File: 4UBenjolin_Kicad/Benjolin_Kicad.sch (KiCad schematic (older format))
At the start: 127 parts, among them J1 Conn_01x04_Male, J10 MAINOUT, J11 PWM, J12 RUN, J13 XOR, J14 CV_1, J15 CV_2, J16 Mix_In_3, J17 Mix_In_4, J18 Mixer_Out, J2 Mix_In_1, J3 Mix_In_2, J4 EXT.INPUT, J5 CV_F, J6 PUL2, J7 TRI1, J8 TRI2, J9 PUL1, Q1 BC547, SW1 SW_SPDT, U1 TL074, U2 TL072, U3 TL074, U4 TL074, U5 SSI2164, U6 4021, U7 L78L09_SOT89, U8 79L09, U9 TL071

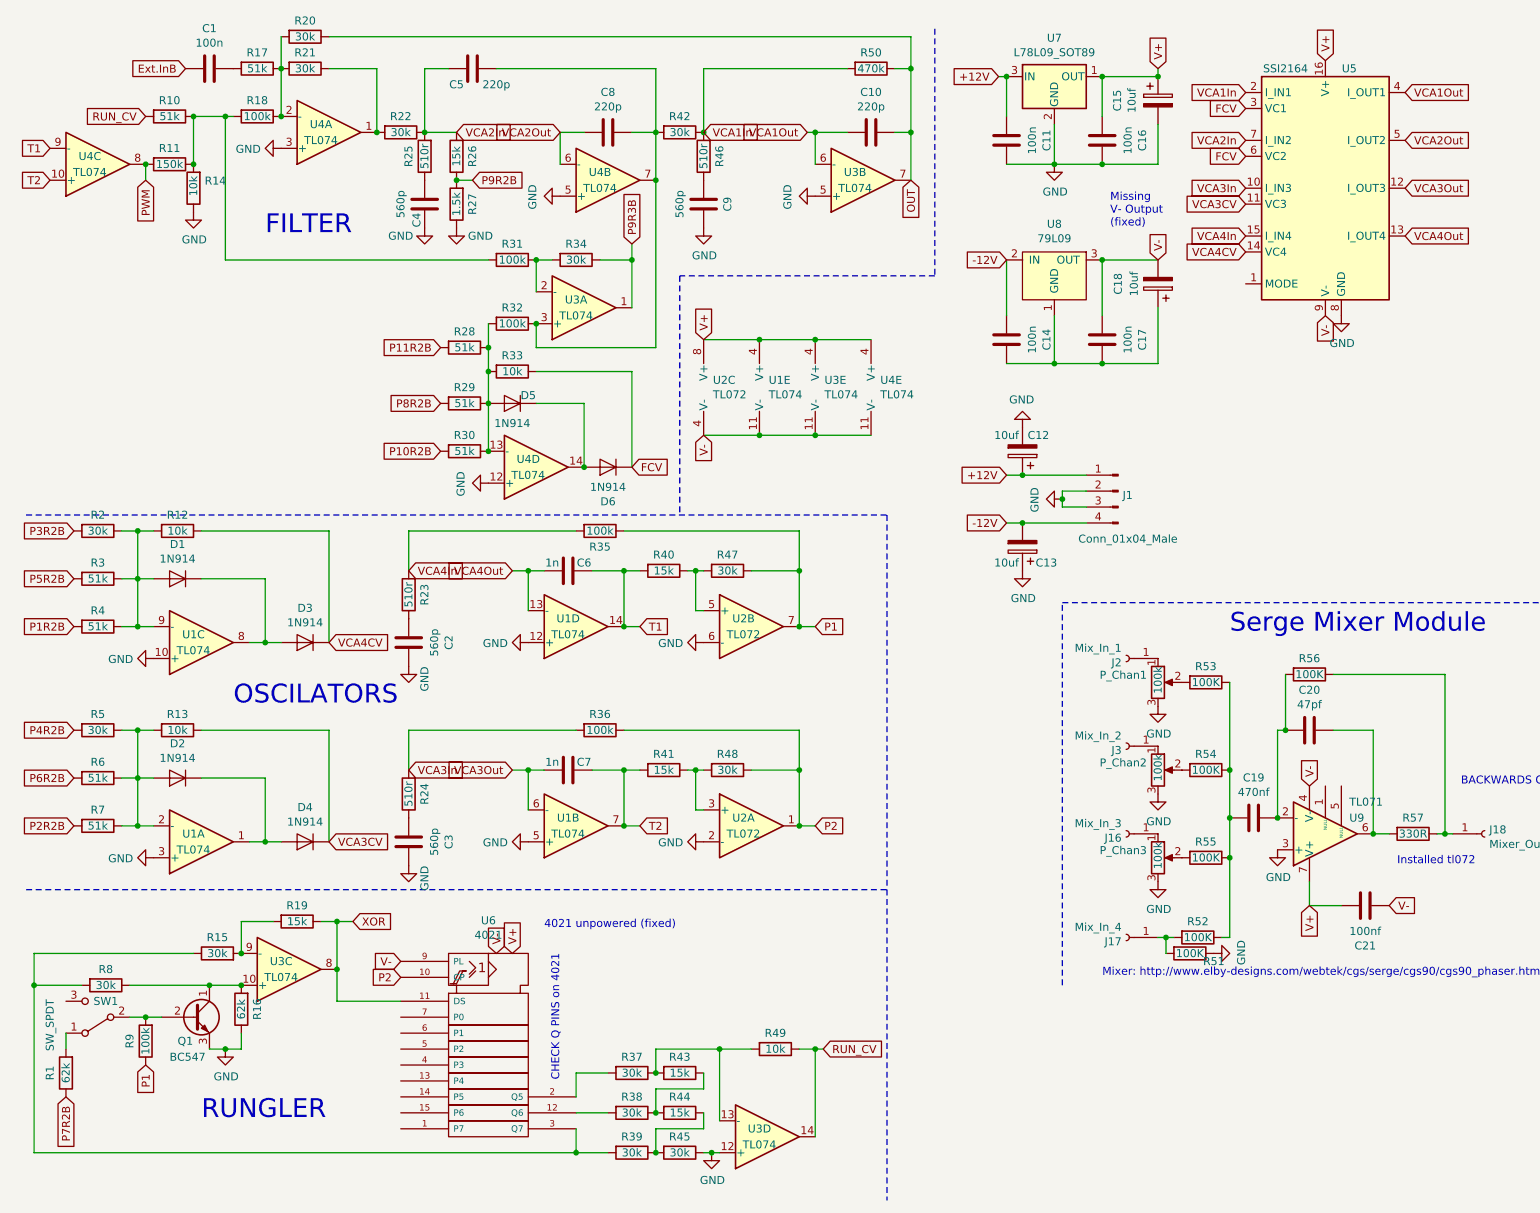
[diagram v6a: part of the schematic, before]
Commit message: Renumbered the resistors. V2 built and sent to jlcpcb
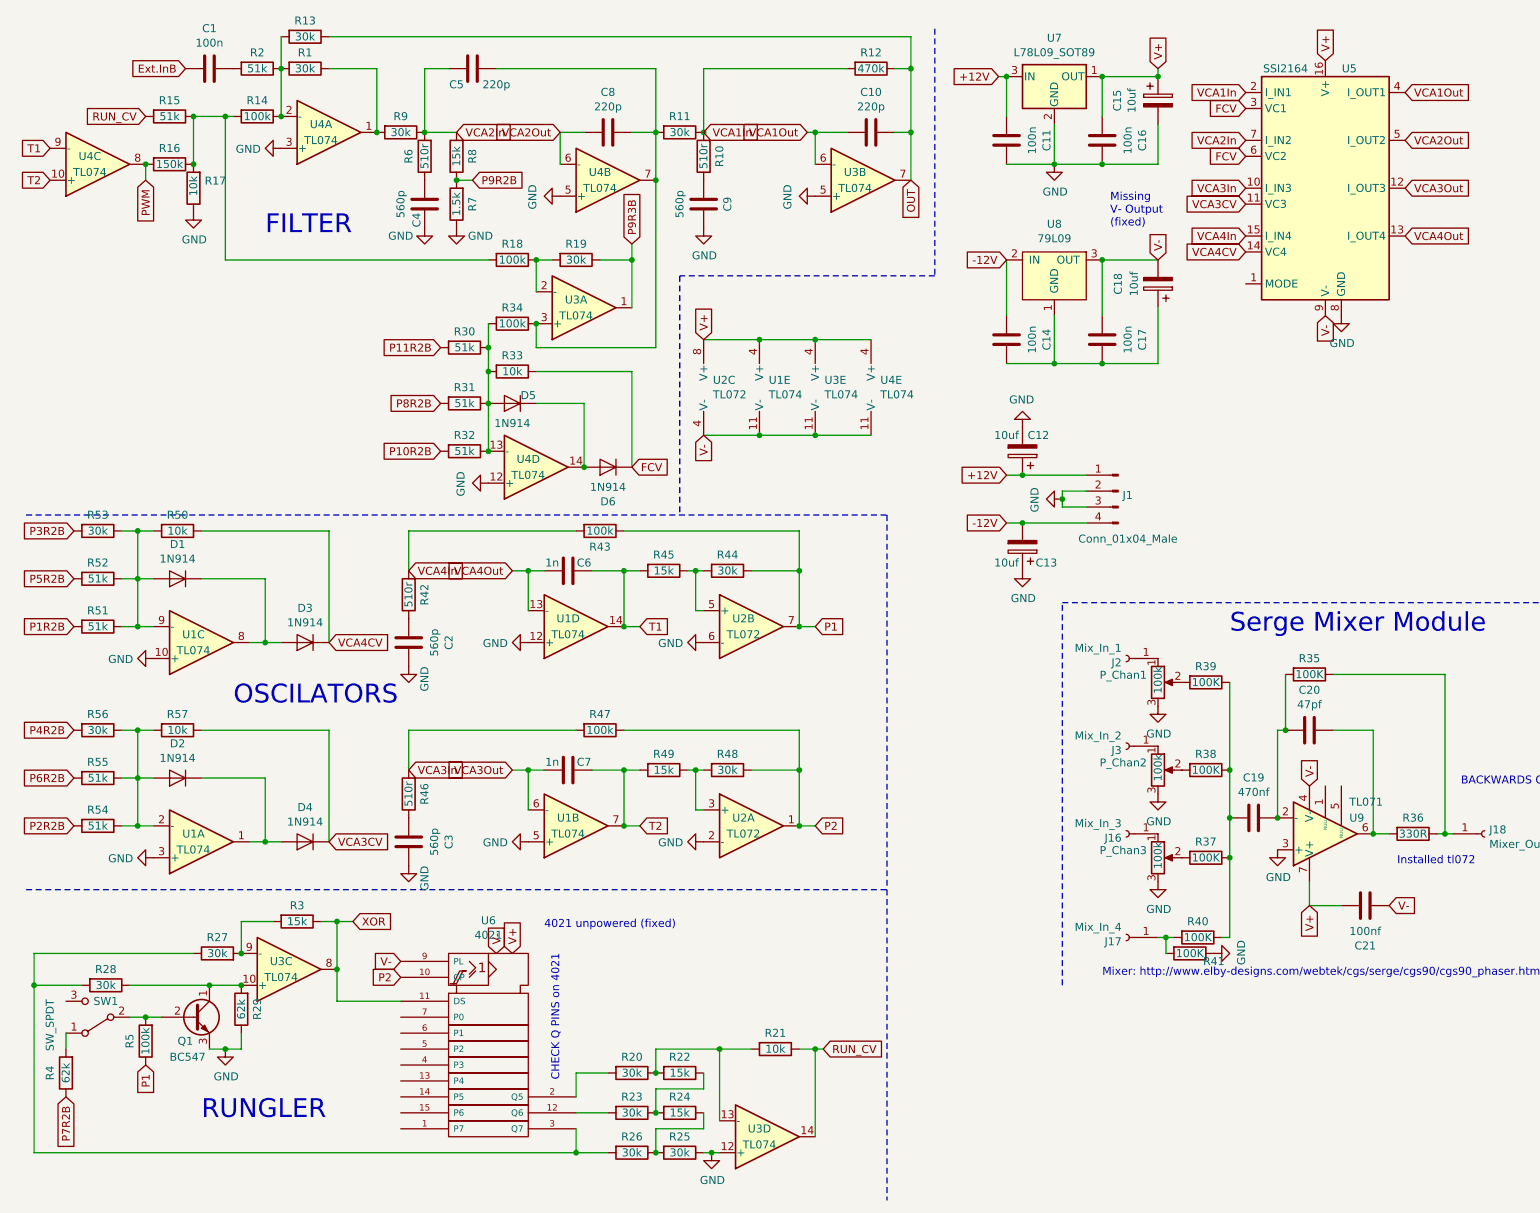
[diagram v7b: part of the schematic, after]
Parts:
- renumbered R21 to R1, R46 to R10, R42 to R11, R50 to R12, R20 to R13, R18 to R14, R10 to R15, R11 to R16, R14 to R17, R31 to R18, R34 to R19, R17 to R2, R37 to R20, R49 to R21, R43 to R22, R38 to R23, R44 to R24, R45 to R25, R39 to R26, R15 to R27, R8 to R28, R16 to R29, R19 to R3, R28 to R30, R29 to R31, R30 to R32, R32 to R34, R56 to R35, R57 to R36, R55 to R37, R54 to R38, R53 to R39, R1 to R4, R52 to R40, R51 to R41, R23 to R42, R35 to R43, R47 to R44, R40 to R45, R24 to R46, R36 to R47, R41 to R49, R9 to R5, R12 to R50, R4 to R51, R3 to R52, R2 to R53, R7 to R54, R6 to R55, R5 to R56, R13 to R57, R25 to R6, R27 to R7, R26 to R8, R22 to R9
